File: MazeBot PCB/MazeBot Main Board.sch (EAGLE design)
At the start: 43 parts, among them IC1 7805TV, IC2 L298, Q1 16MHz

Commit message: Route PCB with SMD
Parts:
- renumbered PWR_LED to PWR, RX_LED to RX, SLOT_SENS_L to SLOT_L, SLOT_SENS_R to SLOT_R, TX_LED to TX
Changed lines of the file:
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@@
 <part name="P+8" library="supply1" library_urn="urn:adsk.eagle:library:371" deviceset="+5V" device=""/>
 <part name="R4" library="eagle-ltspice" library_urn="urn:adsk.eagle:library:217" deviceset="R" device="R1206" package3d_urn="urn:adsk.eagle:package:13301/1" value="1k"/>
-<part name="PWR_LED" library="led" library_urn="urn:adsk.eagle:library:259" deviceset="LED" device="CHIP-LED0805" package3d_urn="urn:adsk.eagle:package:15818/2"/>
+<part name="PWR" library="led" library_urn="urn:adsk.eagle:library:259" deviceset="LED" device="CHIP-LED0805" package3d_urn="urn:adsk.eagle:package:15818/2"/>
 <part name="GND17" library="supply1" library_urn="urn:adsk.eagle:library:371" deviceset="GND" device=""/>
 <part name="P+9" library="supply1" library_urn="urn:adsk.eagle:library:371" deviceset="+5V" device=""/>
 <part name="R5" library="eagle-ltspice" library_urn="urn:adsk.eagle:library:217" deviceset="R" device="R1206" package3d_urn="urn:adsk.eagle:package:13301/1" value="1k"/>
-<part name="TX_LED" library="led" library_urn="urn:adsk.eagle:library:259" deviceset="LED" device="CHIP-LED0805" package3d_urn="urn:adsk.eagle:package:15818/2"/>
+<part name="TX" library="led" library_urn="urn:adsk.eagle:library:259" deviceset="LED" device="CHIP-LED0805" package3d_urn="urn:adsk.eagle:package:15818/2"/>
 <part name="P+10" library="supply1" library_urn="urn:adsk.eagle:library:371" deviceset="+5V" device=""/>
 <part name="R6" library="eagle-ltspice" library_urn="urn:adsk.eagle:library:217" deviceset="R" device="R1206" package3d_urn="urn:adsk.eagle:package:13301/1" value="1k"/>
-<part name="RX_LED" library="led" library_urn="urn:adsk.eagle:library:259" deviceset="LED" device="CHIP-LED0805" package3d_urn="urn:adsk.eagle:package:15818/2"/>
+<part name="RX" library="led" library_urn="urn:adsk.eagle:library:259" deviceset="LED" device="CHIP-LED0805" package3d_urn="urn:adsk.eagle:package:15818/2"/>
 <part name="IR_RCV" library="SparkFun-Sensors" deviceset="TSOP382" device="38" value="38kHz"/>
 <part name="C10" library="rcl" library_urn="urn:adsk.eagle:library:334" deviceset="CPOL-EU" device="UD-6,3X8,8" package3d_urn="urn:adsk.eagle:package:23471/1" value="4.7uF"/>
@@
 <part name="P+12" library="supply1" library_urn="urn:adsk.eagle:library:371" deviceset="+5V" device=""/>
 <part name="GND19" library="supply1" library_urn="urn:adsk.eagle:library:371" deviceset="GND" device=""/>
-<part name="SLOT_SENS_R" library="con-lstb" library_urn="urn:adsk.eagle:library:162" deviceset="MA03-1" device="" package3d_urn="urn:adsk.eagle:package:8339/1"/>
+<part name="SLOT_R" library="con-lstb" library_urn="urn:adsk.eagle:library:162" deviceset="MA03-1" device="" package3d_urn="urn:adsk.eagle:package:8339/1"/>
 <part name="P+13" library="supply1" library_urn="urn:adsk.eagle:library:371" deviceset="+5V" device=""/>
 <part name="GND20" library="supply1" library_urn="urn:adsk.eagle:library:371" deviceset="GND" device=""/>
-<part name="SLOT_SENS_L" library="con-lstb" library_urn="urn:adsk.eagle:library:162" deviceset="MA03-1" device="" package3d_urn="urn:adsk.eagle:package:8339/1"/>
+<part name="SLOT_L" library="con-lstb" library_urn="urn:adsk.eagle:library:162" deviceset="MA03-1" device="" package3d_urn="urn:adsk.eagle:package:8339/1"/>
 <part name="P+14" library="supply1" library_urn="urn:adsk.eagle:library:371" deviceset="+5V" device=""/>
 <part name="GND21" library="supply1" library_urn="urn:adsk.eagle:library:371" deviceset="GND" device=""/>
@@
 <attribute name="VALUE" x="92.202" y="153.67" size="1.778" layer="96" rot="R90"/>
 </instance>
-<instance part="PWR_LED" gate="G$1" x="88.9" y="144.78" smashed="yes">
+<instance part="PWR" gate="G$1" x="88.9" y="144.78" smashed="yes">
 <attribute name="NAME" x="92.456" y="137.668" size="1.778" layer="95" rot="R90"/>
 <attribute name="VALUE" x="94.615" y="140.208" size="1.778" layer="96" rot="R90"/>
@@
 <attribute name="VALUE" x="102.362" y="153.67" size="1.778" layer="96" rot="R90"/>
 </instance>
-<instance part="TX_LED" gate="G$1" x="99.06" y="144.78" smashed="yes">
+<instance part="TX" gate="G$1" x="99.06" y="144.78" smashed="yes">
 <attribute name="NAME" x="102.616" y="140.208" size="1.778" layer="95" rot="R90"/>
 <attribute name="VALUE" x="104.775" y="140.208" size="1.778" layer="96" rot="R90"/>
@@
 <attribute name="VALUE" x="112.522" y="153.67" size="1.778" layer="96" rot="R90"/>
 </instance>
-<instance part="RX_LED" gate="G$1" x="109.22" y="144.78" smashed="yes">
+<instance part="RX" gate="G$1" x="109.22" y="144.78" smashed="yes">
 <attribute name="NAME" x="112.776" y="140.208" size="1.778" layer="95" rot="R90"/>
 <attribute name="VALUE" x="114.935" y="140.208" size="1.778" layer="96" rot="R90"/>
@@
 <attribute name="VALUE" x="180.34" y="30.48" size="1.778" layer="96"/>
 </instance>
-<instance part="SLOT_SENS_R" gate="G$1" x="241.3" y="40.64" smashed="yes" rot="R180">
+<instance part="SLOT_R" gate="G$1" x="241.3" y="40.64" smashed="yes" rot="R180">
 <attribute name="VALUE" x="242.57" y="48.26" size="1.778" layer="96" rot="R180"/>
 <attribute name="NAME" x="245.11" y="50.038" size="1.778" layer="95" rot="R180"/>
@@
 <attribute name="VALUE" x="220.98" y="30.48" size="1.778" layer="96"/>
 </instance>
-<instance part="SLOT_SENS_L" gate="G$1" x="241.3" y="66.04" smashed="yes" rot="R180">
+<instance part="SLOT_L" gate="G$1" x="241.3" y="66.04" smashed="yes" rot="R180">
 <attribute name="VALUE" x="242.57" y="73.66" size="1.778" layer="96" rot="R180"/>
 <attribute name="NAME" x="245.11" y="75.438" size="1.778" layer="95" rot="R180"/>
@@
 </segment>
 <segment>
-<pinref part="SLOT_SENS_R" gate="G$1" pin="1"/>
+<pinref part="SLOT_R" gate="G$1" pin="1"/>
 <wire x1="233.68" y1="43.18" x2="223.52" y2="43.18" width="0.1524" layer="91"/>
 <wire x1="223.52" y1="43.18" x2="223.52" y2="45.72" width="0.1524" layer="91"/>
@@
 </segment>
 <segment>
-<pinref part="SLOT_SENS_L" gate="G$1" pin="1"/>
+<pinref part="SLOT_L" gate="G$1" pin="1"/>
 <wire x1="233.68" y1="68.58" x2="223.52" y2="68.58" width="0.1524" layer="91"/>
 <wire x1="223.52" y1="68.58" x2="223.52" y2="71.12" width="0.1524" layer="91"/>
@@
 </segment>
 <segment>
-<pinref part="PWR_LED" gate="G$1" pin="C"/>
+<pinref part="PWR" gate="G$1" pin="C"/>
 <wire x1="88.9" y1="139.7" x2="88.9" y2="134.62" width="0.1524" layer="91"/>
 <pinref part="GND17" gate="1" pin="GND"/>
@@
 </segment>
 <segment>
-<pinref part="SLOT_SENS_R" gate="G$1" pin="3"/>
+<pinref part="SLOT_R" gate="G$1" pin="3"/>
 <wire x1="233.68" y1="38.1" x2="223.52" y2="38.1" width="0.1524" layer="91"/>
 <wire x1="223.52" y1="38.1" x2="223.52" y2="35.56" width="0.1524" layer="91"/>
@@
 </segment>
 <segment>
-<pinref part="SLOT_SENS_L" gate="G$1" pin="3"/>
+<pinref part="SLOT_L" gate="G$1" pin="3"/>
 <wire x1="233.68" y1="63.5" x2="223.52" y2="63.5" width="0.1524" layer="91"/>
 <wire x1="223.52" y1="63.5" x2="223.52" y2="60.96" width="0.1524" layer="91"/>
@@
 </segment>
 <segment>
-<pinref part="RX_LED" gate="G$1" pin="C"/>
+<pinref part="RX" gate="G$1" pin="C"/>
 <wire x1="109.22" y1="139.7" x2="109.22" y2="132.08" width="0.1524" layer="91"/>
 <label x="106.68" y="132.08" size="1.778" layer="95" rot="R90"/>
@@
 </segment>
 <segment>
-<pinref part="SLOT_SENS_R" gate="G$1" pin="2"/>
+<pinref part="SLOT_R" gate="G$1" pin="2"/>
 <wire x1="233.68" y1="40.64" x2="223.52" y2="40.64" width="0.1524" layer="91"/>
 <label x="215.9" y="40.64" size="1.778" layer="95"/>
@@
 </segment>
 <segment>
-<pinref part="SLOT_SENS_L" gate="G$1" pin="2"/>
+<pinref part="SLOT_L" gate="G$1" pin="2"/>
 <wire x1="233.68" y1="66.04" x2="223.52" y2="66.04" width="0.1524" layer="91"/>
 <label x="215.9" y="66.04" size="1.778" layer="95"/>
@@
 <segment>
 <pinref part="R4" gate="G$1" pin="1"/>
-<pinref part="PWR_LED" gate="G$1" pin="A"/>
+<pinref part="PWR" gate="G$1" pin="A"/>
 <wire x1="88.9" y1="149.86" x2="88.9" y2="147.32" width="0.1524" layer="91"/>
 </segment>
@@
 <segment>
 <pinref part="R5" gate="G$1" pin="1"/>
-<pinref part="TX_LED" gate="G$1" pin="A"/>
+<pinref part="TX" gate="G$1" pin="A"/>
 <wire x1="99.06" y1="149.86" x2="99.06" y2="147.32" width="0.1524" layer="91"/>
 </segment>
@@
 <segment>
 <pinref part="R6" gate="G$1" pin="1"/>
-<pinref part="RX_LED" gate="G$1" pin="A"/>
+<pinref part="RX" gate="G$1" pin="A"/>
 <wire x1="109.22" y1="149.86" x2="109.22" y2="147.32" width="0.1524" layer="91"/>
 </segment>
@@
 </segment>
 <segment>
-<pinref part="TX_LED" gate="G$1" pin="C"/>
+<pinref part="TX" gate="G$1" pin="C"/>
 <wire x1="99.06" y1="139.7" x2="99.06" y2="132.08" width="0.1524" layer="91"/>
 <label x="96.52" y="129.54" size="1.778" layer="95" rot="R90"/>

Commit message: Fix libraries nums on pads
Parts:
- IC2: device st-microelectronics:L298 -> EAGLE_std_edits_MZ:L298
- SERVO, SLOT_L, SLOT_R: device con-lstb:MA03-1 -> EAGLE_std_edits_MZ:MA03-1
- ULTR_SENSOR: device con-lstb:MA04-1 -> EAGLE_std_edits_MZ:MA04-1
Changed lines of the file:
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@@
 <part name="GND4" library="supply1" library_urn="urn:adsk.eagle:library:371" deviceset="GND" device=""/>
 <part name="GND5" library="supply1" library_urn="urn:adsk.eagle:library:371" deviceset="GND" device=""/>
-<part name="IC2" library="st-microelectronics" library_urn="urn:adsk.eagle:library:368" deviceset="L298" device="" package3d_urn="urn:adsk.eagle:package:26823/1"/>
+<part name="IC2" library="EAGLE_std_edits_MZ" deviceset="L298" device="" package3d_urn="urn:adsk.eagle:package:26823/1"/>
 <part name="P+3" library="supply1" library_urn="urn:adsk.eagle:library:371" deviceset="V+" device=""/>
 <part name="P+4" library="supply1" library_urn="urn:adsk.eagle:library:371" deviceset="+5V" device=""/>
@@
 <part name="P+11" library="supply1" library_urn="urn:adsk.eagle:library:371" deviceset="+5V" device=""/>
 <part name="GND18" library="supply1" library_urn="urn:adsk.eagle:library:371" deviceset="GND" device=""/>
-<part name="ULTR_SENSOR" library="con-lstb" library_urn="urn:adsk.eagle:library:162" deviceset="MA04-1" device="" package3d_urn="urn:adsk.eagle:package:8337/1"/>
+<part name="ULTR_SENSOR" library="EAGLE_std_edits_MZ" deviceset="MA04-1" device="" package3d_urn="urn:adsk.eagle:package:8337/1"/>
 <part name="P+12" library="supply1" library_urn="urn:adsk.eagle:library:371" deviceset="+5V" device=""/>
 <part name="GND19" library="supply1" library_urn="urn:adsk.eagle:library:371" deviceset="GND" device=""/>
-<part name="SLOT_R" library="con-lstb" library_urn="urn:adsk.eagle:library:162" deviceset="MA03-1" device="" package3d_urn="urn:adsk.eagle:package:8339/1"/>
+<part name="SLOT_R" library="EAGLE_std_edits_MZ" deviceset="MA03-1" device="" package3d_urn="urn:adsk.eagle:package:8339/1"/>
 <part name="P+13" library="supply1" library_urn="urn:adsk.eagle:library:371" deviceset="+5V" device=""/>
 <part name="GND20" library="supply1" library_urn="urn:adsk.eagle:library:371" deviceset="GND" device=""/>
-<part name="SLOT_L" library="con-lstb" library_urn="urn:adsk.eagle:library:162" deviceset="MA03-1" device="" package3d_urn="urn:adsk.eagle:package:8339/1"/>
+<part name="SLOT_L" library="EAGLE_std_edits_MZ" deviceset="MA03-1" device="" package3d_urn="urn:adsk.eagle:package:8339/1"/>
 <part name="P+14" library="supply1" library_urn="urn:adsk.eagle:library:371" deviceset="+5V" device=""/>
 <part name="GND21" library="supply1" library_urn="urn:adsk.eagle:library:371" deviceset="GND" device=""/>
-<part name="SERVO" library="con-lstb" library_urn="urn:adsk.eagle:library:162" deviceset="MA03-1" device="" package3d_urn="urn:adsk.eagle:package:8339/1"/>
+<part name="SERVO" library="EAGLE_std_edits_MZ" deviceset="MA03-1" device="" package3d_urn="urn:adsk.eagle:package:8339/1"/>
 <part name="C11" library="rcl" library_urn="urn:adsk.eagle:library:334" deviceset="CPOL-EU" device="UD-6,3X8,8" package3d_urn="urn:adsk.eagle:package:23471/1" value="47uF"/>
 <part name="P+15" library="supply1" library_urn="urn:adsk.eagle:library:371" deviceset="+5V" device=""/>

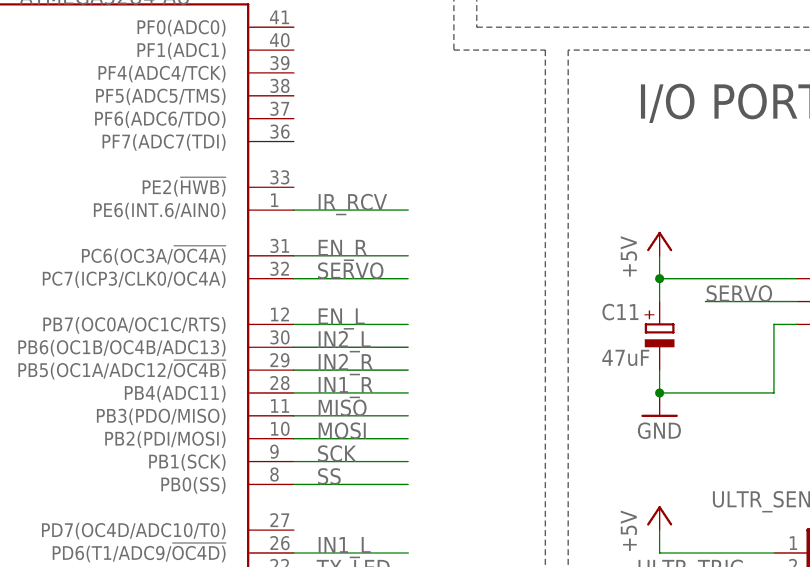
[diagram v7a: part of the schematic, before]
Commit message: Add HWB grounding
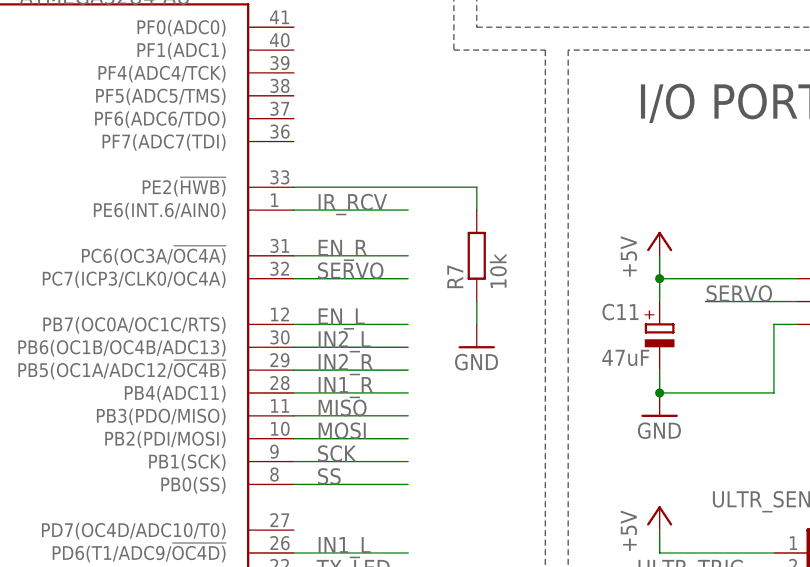
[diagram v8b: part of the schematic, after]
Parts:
- added R7: 10k, eagle-ltspice:RR1206
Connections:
- new net N$8: R7.2, U$1.PE2(!HWB)
- net GND: now also R7.1
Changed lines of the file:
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@@
 <part name="MOT_L" library="adafruit" deviceset="1X2" device="-3.5MM"/>
 <part name="MOT_R" library="adafruit" deviceset="1X2" device="-3.5MM"/>
+<part name="R7" library="eagle-ltspice" library_urn="urn:adsk.eagle:library:217" deviceset="R" device="R1206" package3d_urn="urn:adsk.eagle:package:13301/1" value="10k"/>
+<part name="GND24" library="supply1" library_urn="urn:adsk.eagle:library:371" deviceset="GND" device=""/>
 </parts>
 <sheets>
@@
 <attribute name="NAME" x="236.22" y="86.36" size="1.778" layer="95"/>
 </instance>
+<instance part="R7" gate="G$1" x="162.56" y="78.74" smashed="yes" rot="R90">
+<attribute name="NAME" x="161.0614" y="74.93" size="1.778" layer="95" rot="R90"/>
+<attribute name="VALUE" x="165.862" y="74.93" size="1.778" layer="96" rot="R90"/>
+</instance>
+<instance part="GND24" gate="1" x="162.56" y="68.58" smashed="yes">
+<attribute name="VALUE" x="160.02" y="66.04" size="1.778" layer="96"/>
+</instance>
 </instances>
 <busses>
@@
 <pinref part="GND23" gate="1" pin="GND"/>
 <pinref part="PWR_IN" gate="G$1" pin="1"/>
+</segment>
+<segment>
+<pinref part="R7" gate="G$1" pin="1"/>
+<pinref part="GND24" gate="1" pin="GND"/>
+<wire x1="162.56" y1="73.66" x2="162.56" y2="71.12" width="0.1524" layer="91"/>
 </segment>
 </net>
@@
 </segment>
 </net>
+<net name="N$8" class="0">
+<segment>
+<pinref part="U$1" gate="G$1" pin="PE2(!HWB)"/>
+<wire x1="142.24" y1="86.36" x2="162.56" y2="86.36" width="0.1524" layer="91"/>
+<wire x1="162.56" y1="86.36" x2="162.56" y2="83.82" width="0.1524" layer="91"/>
+<pinref part="R7" gate="G$1" pin="2"/>
+</segment>
+</net>
